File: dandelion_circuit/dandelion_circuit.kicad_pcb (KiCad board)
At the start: 4 copper layers, 100.4 x 42.7 mm, 116 parts, among them J1 MOLEX 733910083, J2 USB_B_Micro, J3 Conn_01x02, J4 Screw_Terminal_01x10, J5 Conn_01x04_Male, J6 Conn_01x02, Q1 SSM3J332R, SW1 Reset, SW2 BTN 1, SW3 SW_DIP_x03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

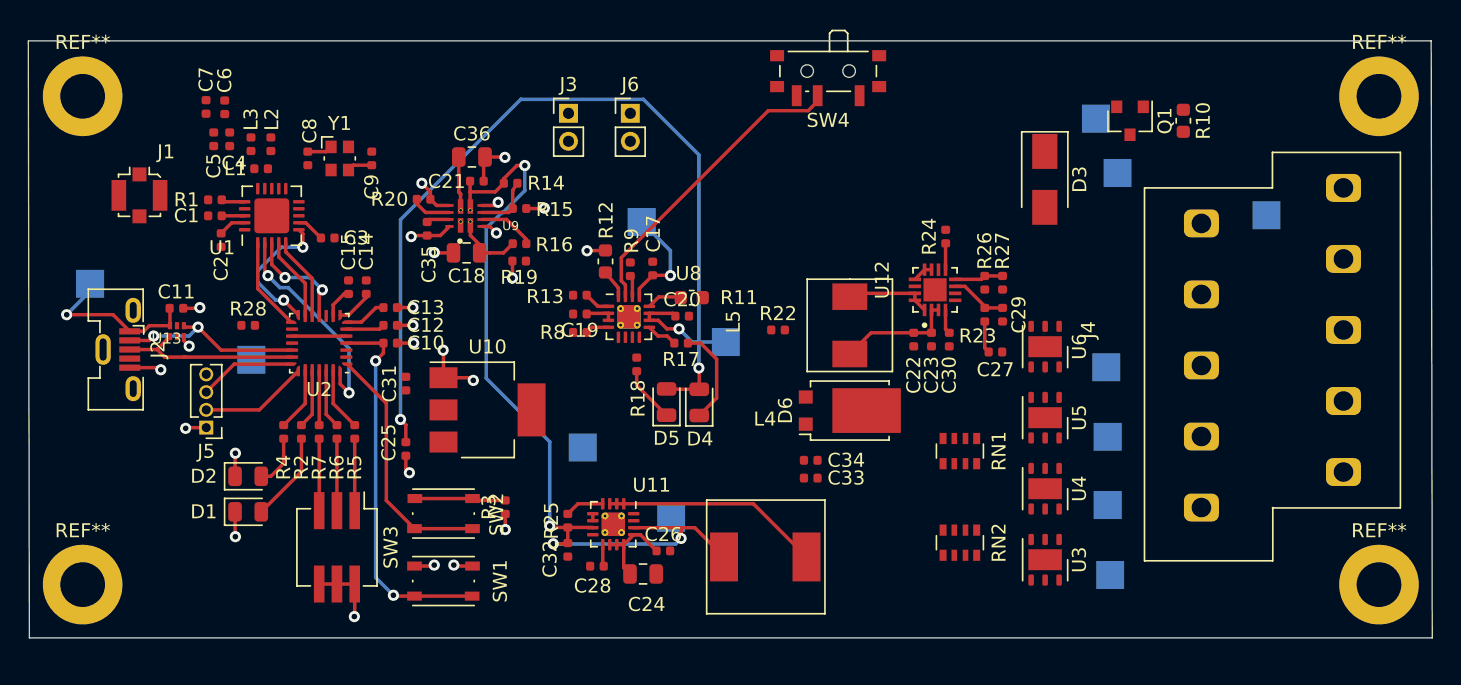
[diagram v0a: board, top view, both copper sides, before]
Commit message: Finished all the routing for SLAVE NODE
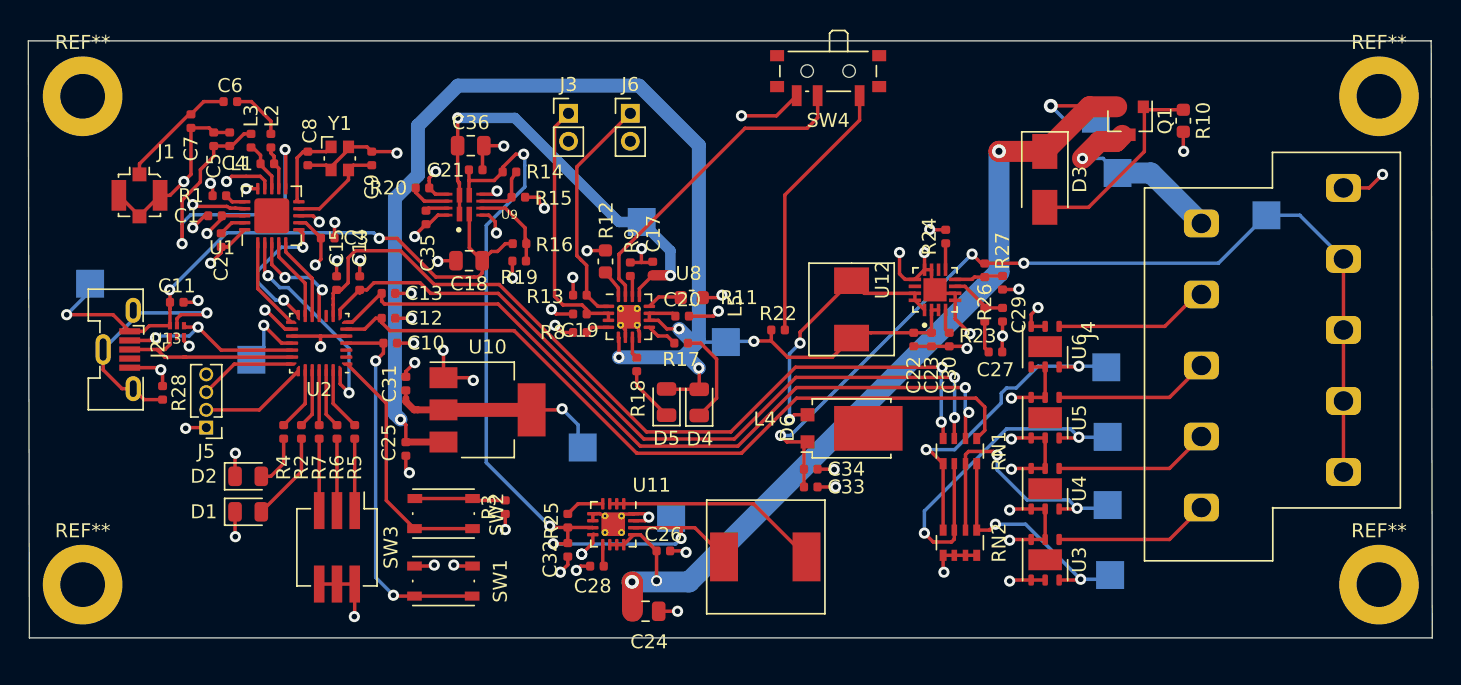
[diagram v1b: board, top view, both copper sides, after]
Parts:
- moved R28 7.79 mm to (47.6, 80.3), turned to -90 degrees
- moved C24 2.67 mm to (82.2, 95.9)
- moved C7 1.48 mm to (49.7, 60.8), turned to -90 degrees
- moved D6 1.28 mm to (96.9, 82.8)
- moved L5 1.15 mm to (96.9, 74.3)
- moved C13 1.02 mm to (63.8, 73.2)
- moved C15 0.90 mm to (60.1, 72.4)
- moved R26 0.89 mm to (106.4, 71.5), turned to -90 degrees
- moved C21 0.81 mm to (70.0, 64.3)
- moved C35 0.81 mm to (66.5, 67.7)
- moved C36 0.81 mm to (69.7, 62.6)
- moved R15 0.81 mm to (73.1, 66.3)
- moved U9 0.81 mm to (69.2, 66.8)
- moved R14 0.81 mm to (72.4, 64.5)
- moved R20 0.81 mm to (66.2, 65.6)
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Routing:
- net GND: track 46.0 -> 174.6 mm, vias 25 -> 71
- net S_NODE_12V: track 0.00 -> 69.3 mm, vias 0 -> 3
- net S_NODE_SOLAR_OUTPUT: track 6.40 -> 68.5 mm, vias 0 -> 4
- net ADC_3: track 2.22 -> 59.9 mm, vias 0 -> 2
- net ADC_2: track 2.64 -> 56.2 mm, vias 0 -> 2
- net ADC_1: track 3.03 -> 55.5 mm, vias 0 -> 2
- net ADC_0: track 2.77 -> 54.5 mm
- net +3V3: track 7.54 -> 37.6 mm, vias 0 -> 5
- net S_NODE_USB_POWER: track 16.9 -> 46.1 mm, vias 1 -> 3
- net VDD_PA: track 0.00 -> 27.4 mm, vias 0 -> 2
- net ADC_2_IN: track 0.00 -> 26.7 mm, vias 0 -> 2
- net S_NODE_COMBINED_POWER: track 79.2 -> 104.6 mm, vias 3 -> 5
- net ADC_3_IN: track 0.00 -> 23.6 mm, vias 0 -> 2
- net S_NODE_P_MUX_OUT: track 11.4 -> 30.9 mm, vias 1 -> 2
- net ADC_1_IN: track 0.00 -> 19.4 mm, vias 0 -> 2
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- added copper zone on 3.3V, net +3V3
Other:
- net class Solar Power added: clearance 0.2, trace_width 1.5, via_dia 1, via_drill 0.4
- net class combined power added: clearance 0.2, trace_width 1, via_dia 0.8, via_drill 0.4
- net class power mux fix added: clearance 0, trace_width 0.25, via_dia 0.8, via_drill 0.4
